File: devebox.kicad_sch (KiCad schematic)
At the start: 24 parts, among them J1 Conn_01x05, J2 Conn_01x04, J3 Right Header, J4 Left Header, SW1 tact switch, U1 STM32H743VIT6, Y1 25MHZ

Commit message: snapshot
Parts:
- added R12, R13: 33, Resistor_SMD:R_0603_1608Metric_Pad0.98x0.95mm_HandSolder, symbol Device:R_Small
- C1, C10, C4, C5, C6, C7, C8, C9: footprint Capacitor_SMD:C_0805_2012Metric_Pad1.18x1.45mm_HandSolder -> Capacitor_SMD:C_0603_1608Metric_Pad1.08x0.95mm_HandSolder
- C2, C3: footprint Capacitor_SMD:C_0805_2012Metric -> Capacitor_SMD:C_0805_2012Metric_Pad1.18x1.45mm_HandSolder
- J1: value Conn_01x05 -> ST-LINK
- J2: value Conn_01x04 -> USB
- R1: footprint Resistor_SMD:R_0805_2012Metric_Pad1.20x1.40mm_HandSolder -> Resistor_SMD:R_0603_1608Metric_Pad0.98x0.95mm_HandSolder
- R2, R3, R4, R5: footprint Resistor_THT:R_Axial_DIN0207_L6.3mm_D2.5mm_P10.16mm_Horizontal -> Resistor_SMD:R_0603_1608Metric_Pad0.98x0.95mm_HandSolder
- U1: value STM32H743VIT6 -> STM32H743VITx
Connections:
- net +3.3V: now also Y1.1 (Tri-State)
- net PA11: now also R12.1; no longer J2.2 (Pin_2)
- net PA12: now also R13.1; no longer J2.3 (Pin_3)
- new net: J2.2 (Pin_2), R12.2
- new net: J2.3 (Pin_3), R13.2
- no-connect marks 0 -> 6

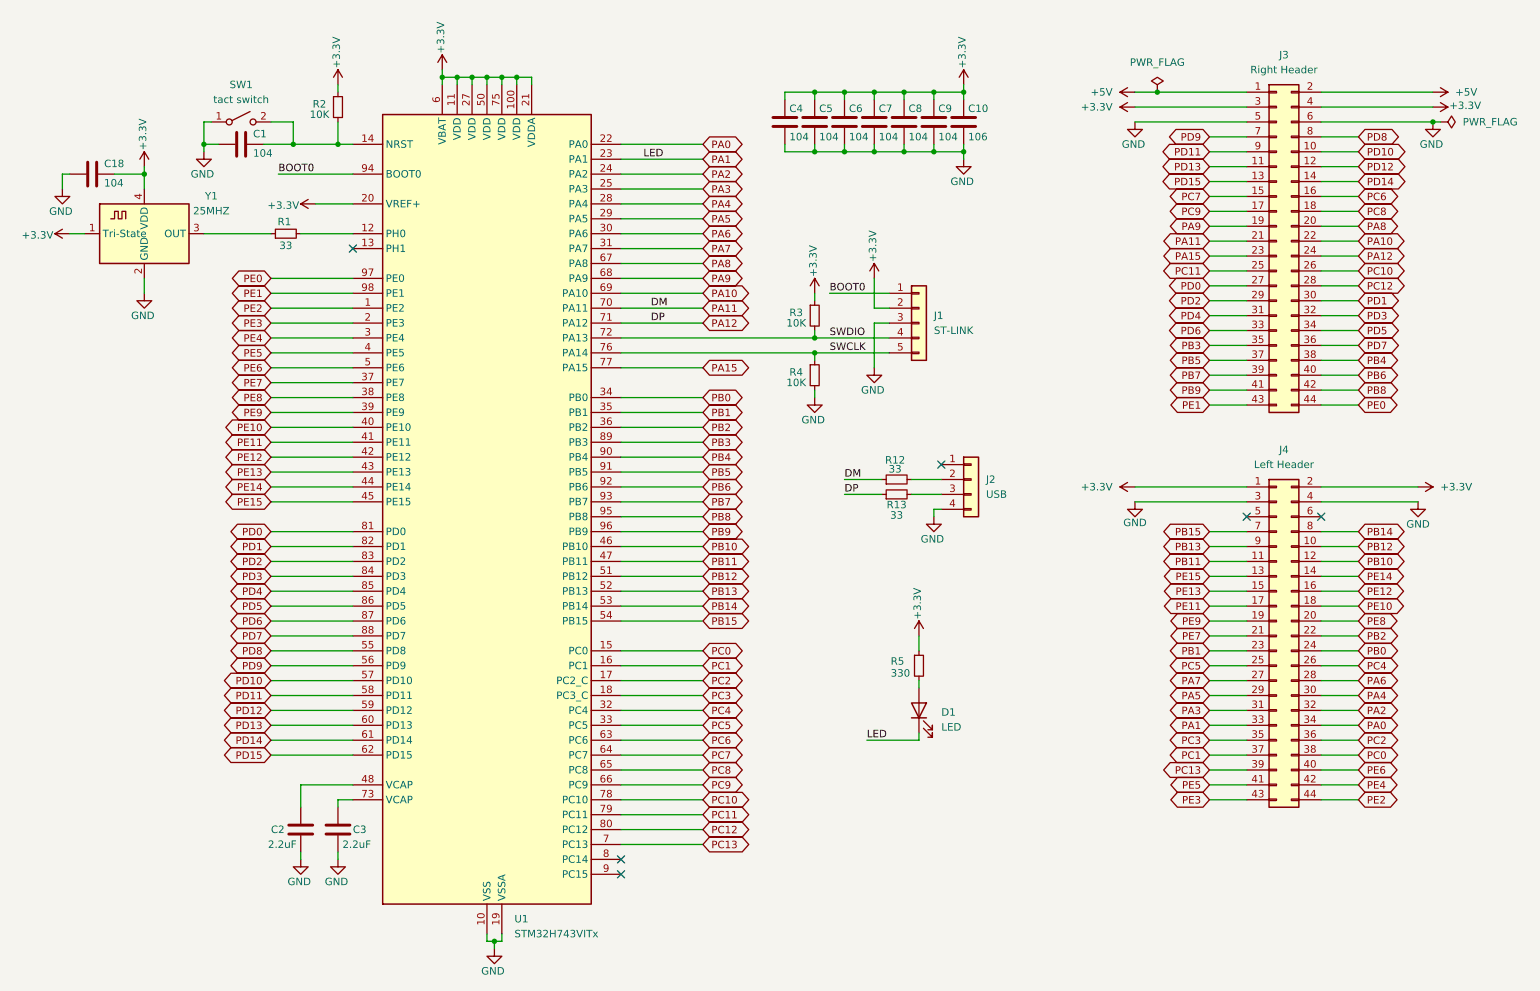
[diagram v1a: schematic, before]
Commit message: add servos and fan outputs
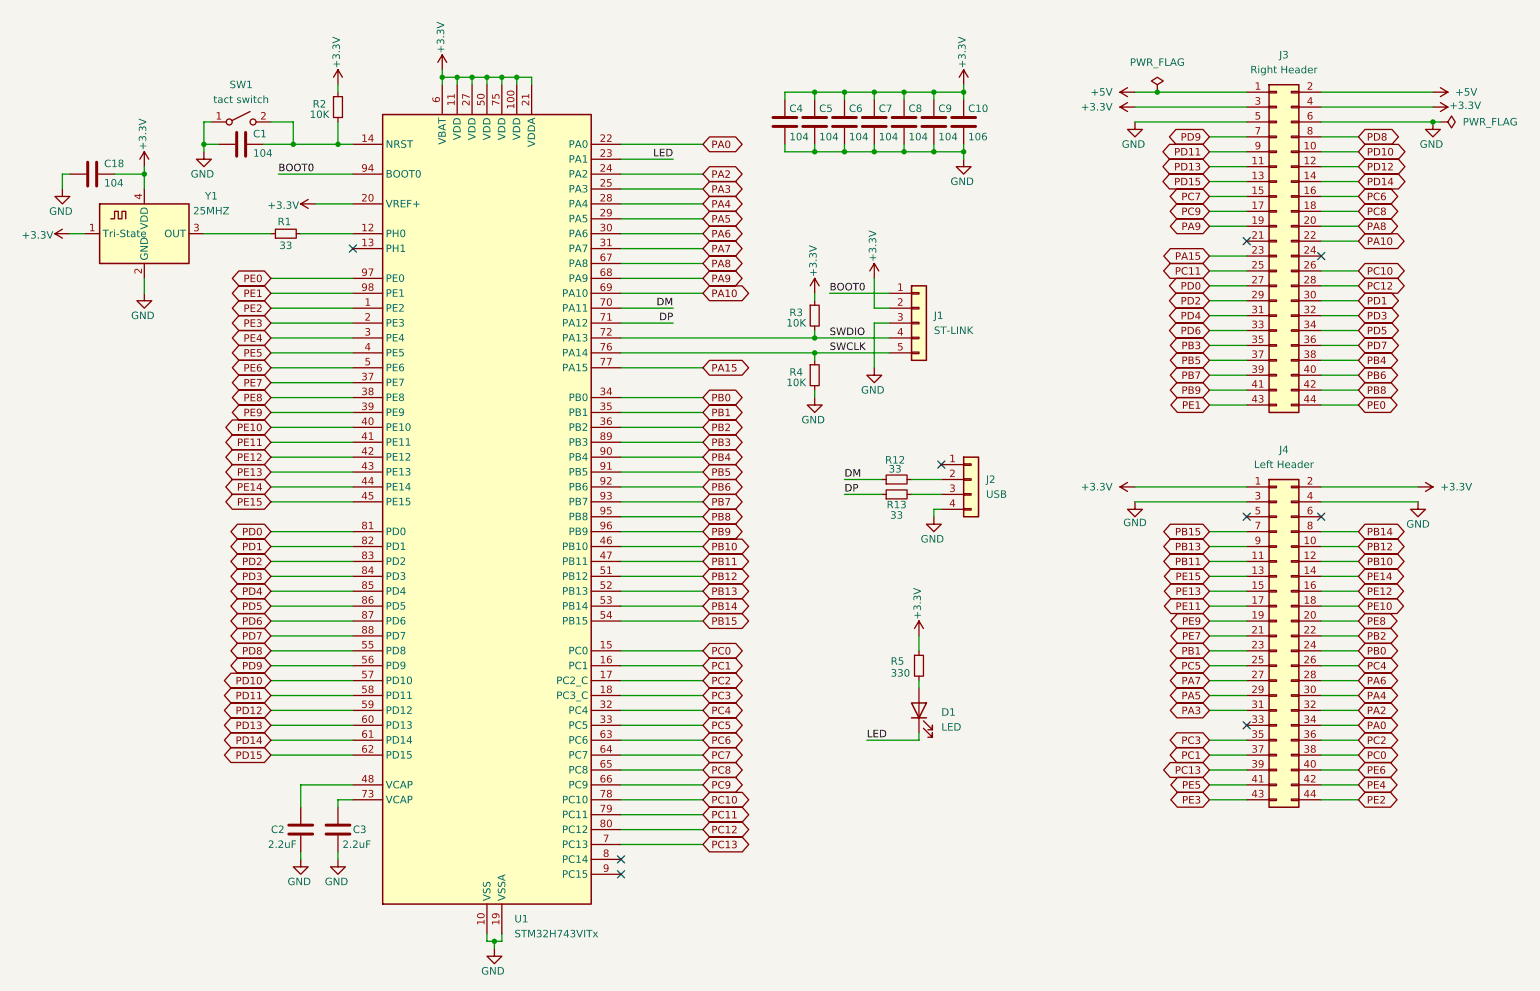
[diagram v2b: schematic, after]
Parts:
- C1, C10, C2, C3, C4, C5, C6, C7, C8, C9: symbol Device:C -> LM2676S-3.3_NOPB:C
- C18: footprint Capacitor_SMD:C_0805_2012Metric_Pad1.18x1.45mm_HandSolder -> Capacitor_SMD:C_0603_1608Metric_Pad1.08x0.95mm_HandSolder; symbol Device:C -> LM2676S-3.3_NOPB:C
- D1: symbol Device:LED -> LM2676S-3.3_NOPB:LED
- J1: symbol Connector_Generic:Conn_01x05 -> LM2676S-3.3_NOPB:Conn_01x05
- J2: symbol Connector_Generic:Conn_01x04 -> LM2676S-3.3_NOPB:Conn_01x04_1
- J3, J4: symbol Connector_Generic:Conn_02x22_Odd_Even -> LM2676S-3.3_NOPB:Conn_02x22_Odd_Even
- R1, R12, R13, R2, R3, R4, R5: footprint Resistor_SMD:R_0603_1608Metric_Pad0.98x0.95mm_HandSolder -> Resistor_SMD:R_0805_2012Metric_Pad1.20x1.40mm_HandSolder; symbol Device:R_Small -> LM2676S-3.3_NOPB:R_Small
- SW1: footprint Button_Switch_THT:Momentary_SMD_4.6x2.8mm -> Button_Switch_THT:SW_PUSH_6mm_H4.3mm; symbol SparkFun-Switch:SPST_Momentary_4.6x2.8mm -> LM2676S-3.3_NOPB:SPST_Momentary_4.6x2.8mm
- U1: symbol MCU_ST_STM32H7:STM32H743VITx -> LM2676S-3.3_NOPB:STM32H743VITx
- Y1: symbol Oscillator:ASCO -> LM2676S-3.3_NOPB:ASCO
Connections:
- net PA1 renamed LED
- net LED: no longer J4.33 (Pin_33)
- net PA11 renamed DM
- net DM: no longer J3.21 (Pin_21)
- net PA12 renamed DP
- net DP: no longer J3.24 (Pin_24)
- no-connect marks 6 -> 9

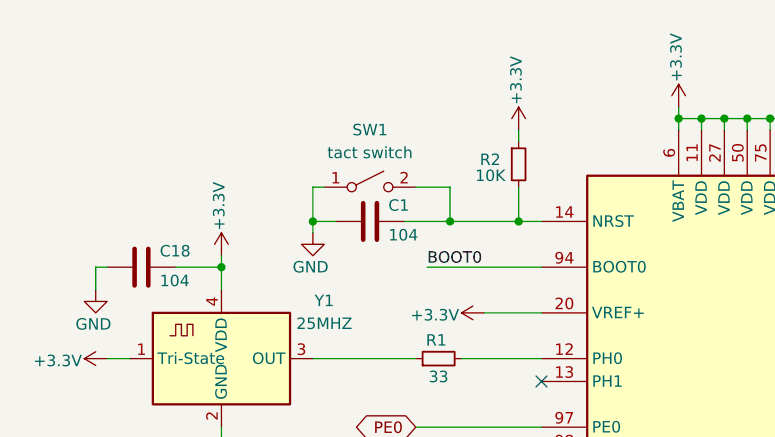
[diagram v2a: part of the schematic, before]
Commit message: change transistors from MMBT2222A to BCP56
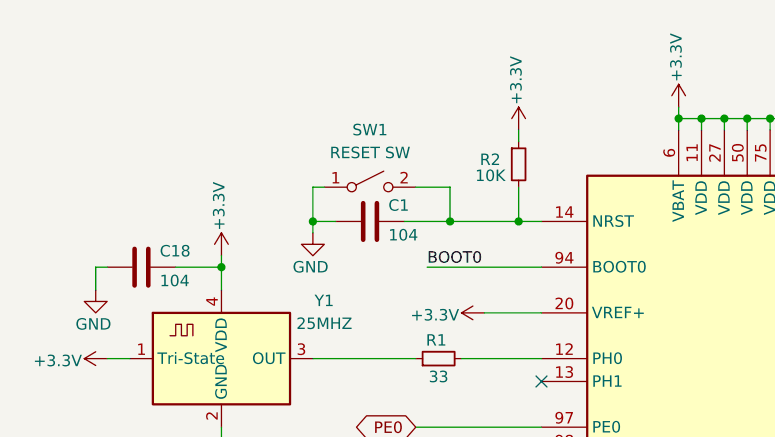
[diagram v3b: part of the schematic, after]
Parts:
- SW1: value tact switch -> RESET SW
- Y1: footprint Oscillator:Oscillator_SMD_Abracon_ASCO-4Pin_1.6x1.2mm -> Oscillator:Oscillator_SMD_Abracon_ASV-4Pin_7.0x5.1mm_HandSoldering
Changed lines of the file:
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@@
 			)
 		)
-		(property "Footprint" "Oscillator:Oscillator_SMD_Abracon_ASCO-4Pin_1.6x1.2mm"
+		(property "Footprint" "Oscillator:Oscillator_SMD_Abracon_ASV-4Pin_7.0x5.1mm_HandSoldering"
 			(at 41.91 62.23 0)
 			(effects
@@
 			)
 		)
-		(property "Value" "tact switch"
+		(property "Value" "RESET SW"
 			(at 55.88 30.48 0)
 			(effects

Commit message: flipped camera connector
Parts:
- added R20: 0, Resistor_SMD:R_0805_2012Metric_Pad1.20x1.40mm_HandSolder, symbol LM2676S-3.3_NOPB:R_Small
- D1: footprint LED_THT:LED_D3.0mm -> LED_SMD:LED_0805_2012Metric_Pad1.15x1.40mm_HandSolder
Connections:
- net +5V: now also R20.1
- net at J2.1 (Pin_1): now also R20.2
- no-connect marks 9 -> 8
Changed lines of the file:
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@@
 	)
 	(no_connect
-		(at 175.26 92.71)
-	)
-	(no_connect
 		(at 240.03 57.15)
 	)
@@
 	(wire
 		(pts
+			(xy 173.99 92.71) (xy 173.99 91.44)
+		)
+		(stroke
+			(width 0)
+			(type default)
+		)
+	)
+	(wire
+		(pts
 			(xy 158.75 97.79) (xy 165.1 97.79)
 		)
@@
 	(wire
 		(pts
+			(xy 173.99 85.09) (xy 173.99 86.36)
+		)
+		(stroke
+			(width 0)
+			(type default)
+		)
+	)
+	(wire
+		(pts
 			(xy 168.91 38.1) (xy 168.91 39.37)
 		)
@@
 	(wire
 		(pts
+			(xy 175.26 92.71) (xy 173.99 92.71)
+		)
+		(stroke
+			(width 0)
+			(type default)
+		)
+	)
+	(wire
+		(pts
 			(xy 60.96 116.84) (xy 74.93 116.84)
 		)
@@
 	)
 	(symbol
+		(lib_id "LM2676S-3.3_NOPB:+5V")
+		(at 173.99 85.09 0)
+		(unit 1)
+		(exclude_from_sim no)
+		(in_bom yes)
+		(on_board yes)
+		(dnp no)
+		(property "Reference" "#PWR070"
+			(at 173.99 88.9 0)
+			(effects
+				(font
+					(size 1.27 1.27)
+				)
+				(hide yes)
+			)
+		)
+		(property "Value" "+5V"
+			(at 173.736 81.28 0)
+			(effects
+				(font
+					(size 1.27 1.27)
+				)
+			)
+		)
+		(property "Footprint" ""
+			(at 173.99 85.09 0)
+			(effects
+				(font
+					(size 1.27 1.27)
+				)
+				(hide yes)
+			)
+		)
+		(property "Datasheet" ""
+			(at 173.99 85.09 0)
+			(effects
+				(font
+					(size 1.27 1.27)
+				)
+				(hide yes)
+			)
+		)
+		(property "Description" "Power symbol creates a global label with name \"+5V\""
+			(at 173.99 85.09 0)
+			(effects
+				(font
+					(size 1.27 1.27)
+				)
+				(hide yes)
+			)
+		)
+		(pin "1"
+		)
+		(instances
+			(project "Main_H743VI"
+				(path "/1c72d2eb-7fb1-49fe-a026-e817f5a7ec43/a876cc3c-46f3-4b62-bd95-490c4538aae6"
+					(reference "#PWR070")
+					(unit 1)
+				)
+			)
+		)
+	)
+	(symbol
 		(lib_id "LM2676S-3.3_NOPB:C")
 		(at 173.99 34.29 0)
@@
 			)
 		)
-		(property "Footprint" "LED_THT:LED_D3.0mm"
+		(property "Footprint" "LED_SMD:LED_0805_2012Metric_Pad1.15x1.40mm_HandSolder"
 			(at 171.45 134.62 0)
 			(effects
@@
 					(unit 1)
 				)
+			)
+		)
+	)
+	(symbol
+		(lib_id "LM2676S-3.3_NOPB:R_Small")
+		(at 173.99 88.9 0)
+		(unit 1)
+		(exclude_from_sim no)
+		(in_bom yes)
+		(on_board yes)
+		(dnp no)
+		(property "Reference" "R20"
+			(at 168.656 88.138 0)
+			(effects
+				(font
+					(size 1.27 1.27)
+				)
+				(justify left)
+			)
+		)
+		(property "Value" "0"
+			(at 169.926 89.916 0)
+			(effects
+				(font
+					(size 1.27 1.27)
+				)
+				(justify left)
+			)
+		)
+		(property "Footprint" "Resistor_SMD:R_0805_2012Metric_Pad1.20x1.40mm_HandSolder"
+			(at 173.99 88.9 0)
+			(effects
+				(font
+					(size 1.27 1.27)
+				)
+				(hide yes)
+			)
+		)
+		(property "Datasheet" "~"
+			(at 173.99 88.9 0)
+			(effects
+				(font
+					(size 1.27 1.27)
+				)
+				(hide yes)
+			)
+		)
+		(property "Description" "Resistor, small symbol"
+			(at 173.99 88.9 0)
+			(effects
+				(font
+					(size 1.27 1.27)
+				)
+				(hide yes)
+			)
+		)
+		(pin "1"
+		)
+		(pin "2"
+		)
+		(instances
+			(project "Main_H743VI"
+				(path "/1c72d2eb-7fb1-49fe-a026-e817f5a7ec43/a876cc3c-46f3-4b62-bd95-490c4538aae6"
+					(reference "R20")
+					(unit 1)
+				)

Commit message: snapshot
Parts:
- added R19: 10K, Resistor_SMD:R_0805_2012Metric_Pad1.20x1.40mm_HandSolder, symbol LM2676S-3.3_NOPB:R_Small
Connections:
- net BOOT0: now also R19.2
- net GND: now also R19.1
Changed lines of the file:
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@@
 	(wire
 		(pts
+			(xy 55.88 43.18) (xy 55.88 44.45)
+		)
+		(stroke
+			(width 0)
+			(type default)
+		)
+	)
+	(wire
+		(pts
 			(xy 62.23 43.18) (xy 74.93 43.18)
 		)
@@
 	(wire
 		(pts
+			(xy 57.15 43.18) (xy 55.88 43.18)
+		)
+		(stroke
+			(width 0)
+			(type default)
+		)
+	)
+	(wire
+		(pts
 			(xy 60.96 139.7) (xy 74.93 139.7)
 		)
@@
 	)
 	(label "BOOT0"
-		(at 62.23 43.18 0)
+		(at 64.77 43.18 0)
 		(effects
 			(font
@@
 		(dnp no)
 		(property "Reference" "C1"
-			(at 57.912 36.322 90)
+			(at 58.166 36.83 90)
 			(effects
 				(font
@@
 		)
 		(property "Value" "104"
-			(at 57.912 39.624 90)
+			(at 57.912 39.116 90)
 			(effects
 				(font
@@
 		(on_board yes)
 		(dnp no)
-		(fields_autoplaced yes)
 		(property "Reference" "Y1"
-			(at 50.8 46.9198 0)
+			(at 43.434 59.944 0)
 			(effects
 				(font
@@
 		)
 		(property "Value" "25MHZ"
-			(at 50.8 49.4598 0)
+			(at 44.196 61.722 0)
 			(effects
 				(font
@@
 	)
 	(symbol
+		(lib_id "LM2676S-3.3_NOPB:GND")
+		(at 55.88 44.45 0)
+		(unit 1)
+		(exclude_from_sim no)
+		(in_bom yes)
+		(on_board yes)
+		(dnp no)
+		(property "Reference" "#PWR071"
+			(at 55.88 50.8 0)
+			(effects
+				(font
+					(size 1.27 1.27)
+				)
+				(hide yes)
+			)
+		)
+		(property "Value" "GND"
+			(at 55.88 48.006 0)
+			(effects
+				(font
+					(size 1.27 1.27)
+				)
+			)
+		)
+		(property "Footprint" ""
+			(at 55.88 44.45 0)
+			(effects
+				(font
+					(size 1.27 1.27)
+				)
+				(hide yes)
+			)
+		)
+		(property "Datasheet" ""
+			(at 55.88 44.45 0)
+			(effects
+				(font
+					(size 1.27 1.27)
+				)
+				(hide yes)
+			)
+		)
+		(property "Description" "Power symbol creates a global label with name \"GND\" , ground"
+			(at 55.88 44.45 0)
+			(effects
+				(font
+					(size 1.27 1.27)
+				)
+				(hide yes)
+			)
+		)
+		(pin "1"
+		)
+		(instances
+			(project "Main_H743VI"
+				(path "/1c72d2eb-7fb1-49fe-a026-e817f5a7ec43/a876cc3c-46f3-4b62-bd95-490c4538aae6"
+					(reference "#PWR071")
+					(unit 1)
+				)
+			)
+		)
+	)
+	(symbol
 		(lib_id "LM2676S-3.3_NOPB:+3.3V")
 		(at 171.45 121.92 0)
@@
 					(unit 1)
 				)
+			)
+		)
+	)
+	(symbol
+		(lib_id "LM2676S-3.3_NOPB:R_Small")
+		(at 59.69 43.18 90)
+		(unit 1)
+		(exclude_from_sim no)
+		(in_bom yes)
+		(on_board yes)
+		(dnp no)
+		(property "Reference" "R19"
+			(at 59.436 41.148 90)
+			(effects
+				(font
+					(size 1.27 1.27)
+				)
+			)
+		)
+		(property "Value" "10K"
+			(at 59.69 45.212 90)
+			(effects
+				(font
+					(size 1.27 1.27)
+				)
+			)
+		)
+		(property "Footprint" "Resistor_SMD:R_0805_2012Metric_Pad1.20x1.40mm_HandSolder"
+			(at 59.69 43.18 0)
+			(effects
+				(font
+					(size 1.27 1.27)
+				)
+				(hide yes)
+			)
+		)
+		(property "Datasheet" "~"
+			(at 59.69 43.18 0)
+			(effects
+				(font
+					(size 1.27 1.27)
+				)
+				(hide yes)
+			)
+		)
+		(property "Description" "Resistor, small symbol"
+			(at 59.69 43.18 0)
+			(effects
+				(font
+					(size 1.27 1.27)
+				)
+				(hide yes)
+			)
+		)
+		(pin "2"
+		)
+		(pin "1"
+		)
+		(instances
+			(project "Main_H743VI"
+				(path "/1c72d2eb-7fb1-49fe-a026-e817f5a7ec43/a876cc3c-46f3-4b62-bd95-490c4538aae6"
+					(reference "R19")
+					(unit 1)
+				)
